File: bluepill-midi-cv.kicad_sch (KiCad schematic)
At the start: 8 parts

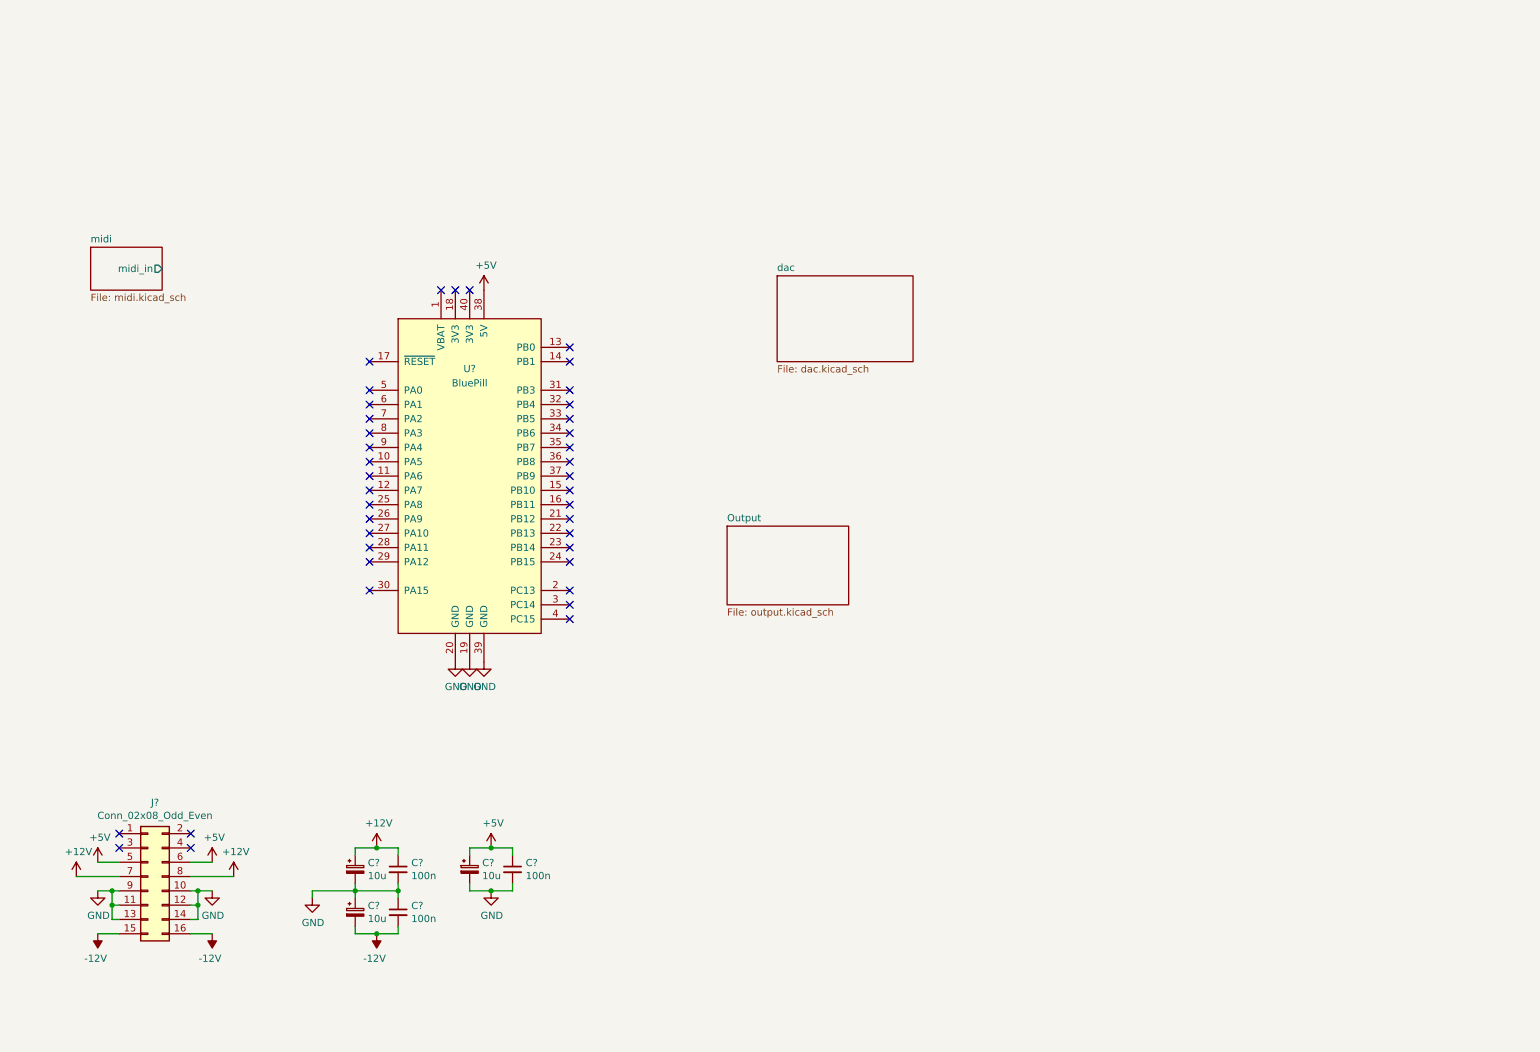
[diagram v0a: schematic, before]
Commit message: move schematic sub-sheets to main sheet
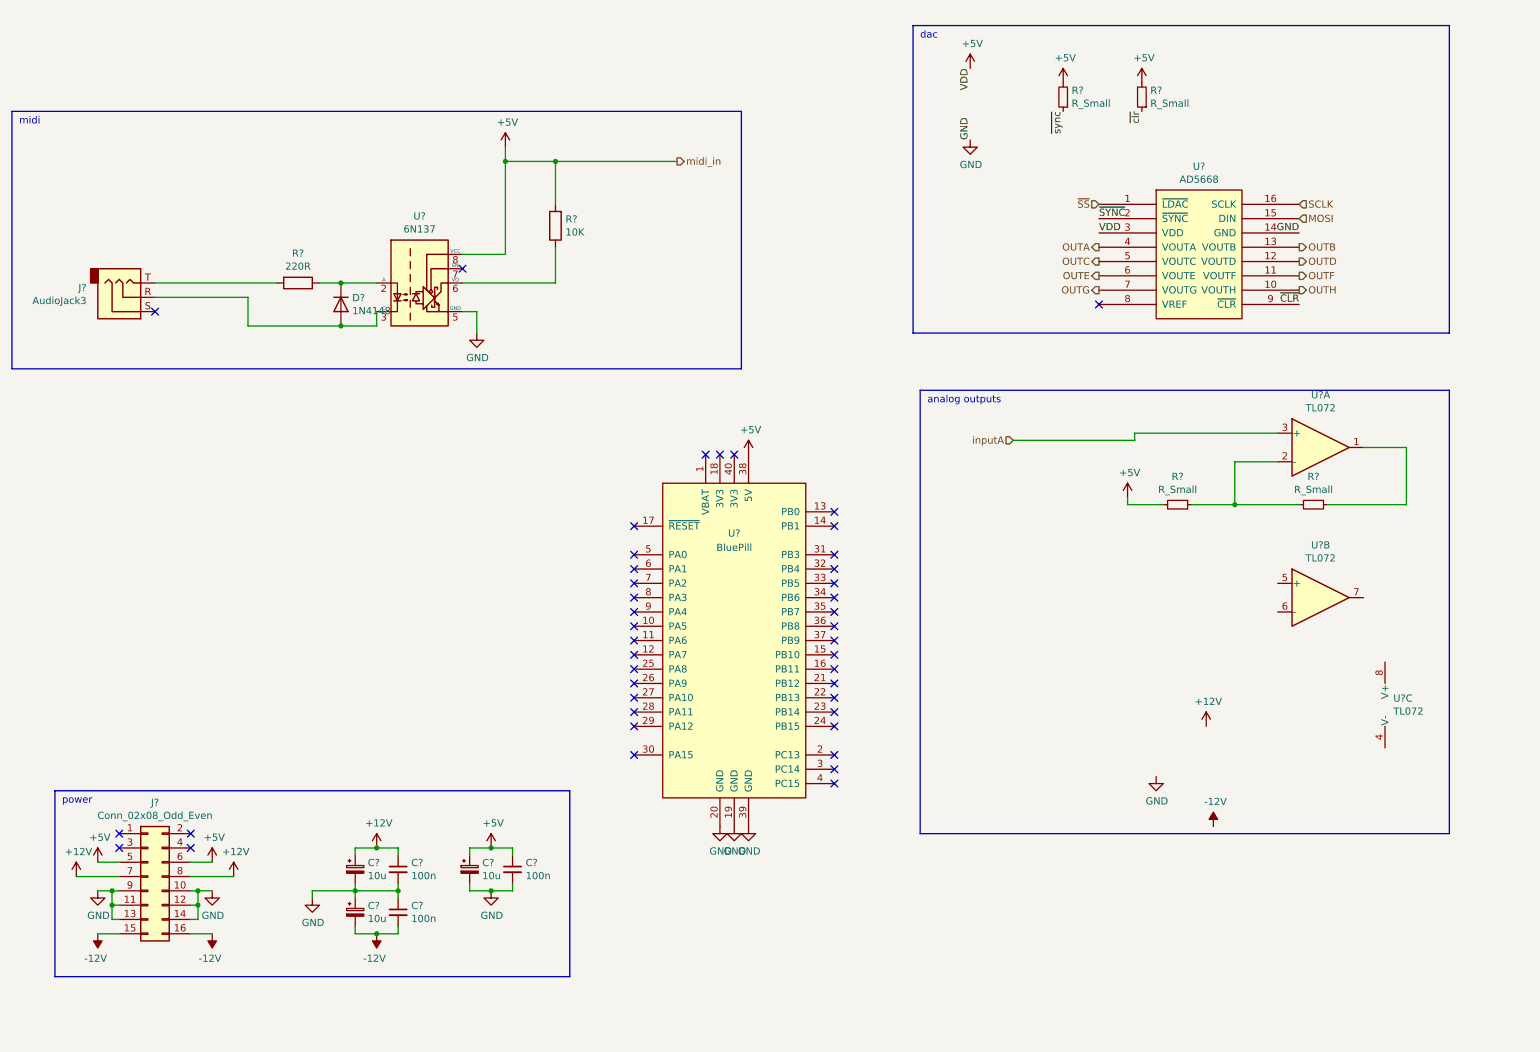
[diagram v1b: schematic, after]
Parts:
- added D?: 1N4148, Diode_SMD:D_0805_2012Metric_Pad1.15x1.40mm_HandSolder, symbol Diode:1N4148
- added J?: AudioJack3, Connector_Audio:Jack_3.5mm_QingPu_WQP-PJ398SM_Vertical_CircularHoles, symbol Connector:AudioJack3
- added R?: 10K, Resistor_SMD:R_0805_2012Metric_Pad1.15x1.40mm_HandSolder, symbol Device:R
- added R? (x4): R_Small, symbol Device:R_Small
- added R?: 220R, Resistor_SMD:R_0805_2012Metric_Pad1.15x1.40mm_HandSolder, symbol Device:R
- added U? (x3): TL072, symbol Amplifier_Operational:TL072
- added U?: AD5668, Package_SO:TSSOP-16-1EP_4.4x5mm_P0.65mm, symbol patchut:AD5668
- added U?: 6N137, Package_DIP:PowerIntegrations_SMD-8, symbol Isolator:6N137
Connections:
- net +5V: now also R?.2, R?.2, R?.2, R?.2, U?.3 (VDD), U?.8 (VCC)
- net GND: now also U?.14 (GND), U?.5 (GND)
- new net: R?.1, U?.6 (VO)
- new net: R?.1, U?.1
- new net: R?.1, R?.2, U?.2 (-)
- new net: D?.1 (K), R?.1, U?.2 (A)
- new net: D?.2 (A), J?.R, U?.3 (C)
- new net: J?.T, R?.2
- new net MOSI: U?.15 (DIN)
- new net OUTA: U?.4 (VOUTA)
- new net OUTB: U?.13 (VOUTB)
- new net OUTC: U?.5 (VOUTC)
- new net OUTD: U?.12 (VOUTD)
- new net OUTE: U?.6 (VOUTE)
- new net OUTF: U?.11 (VOUTF)
- new net OUTG: U?.7 (VOUTG)
- new net OUTH: U?.10 (VOUTH)
- new net SCLK: U?.16 (SCLK)
- new net inputA: U?.3 (+)
- new net ~{CLR}: U?.9 (~{CLR})
- new net ~{SS}: U?.1 (~{LDAC})
- new net ~{SYNC}: U?.2 (~{SYNC})
- new net ~{clr}: R?.1
- new net ~{sync}: R?.1
- no-connect marks 40 -> 43
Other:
- removed sheet Output
- removed sheet dac
- removed sheet midi
- note added: "analog outputs"
- note added: "dac"
- note added: "midi"
- note added: "power"
- moved on the sheet: U?

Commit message: finish 4 analog outs, more cleanup
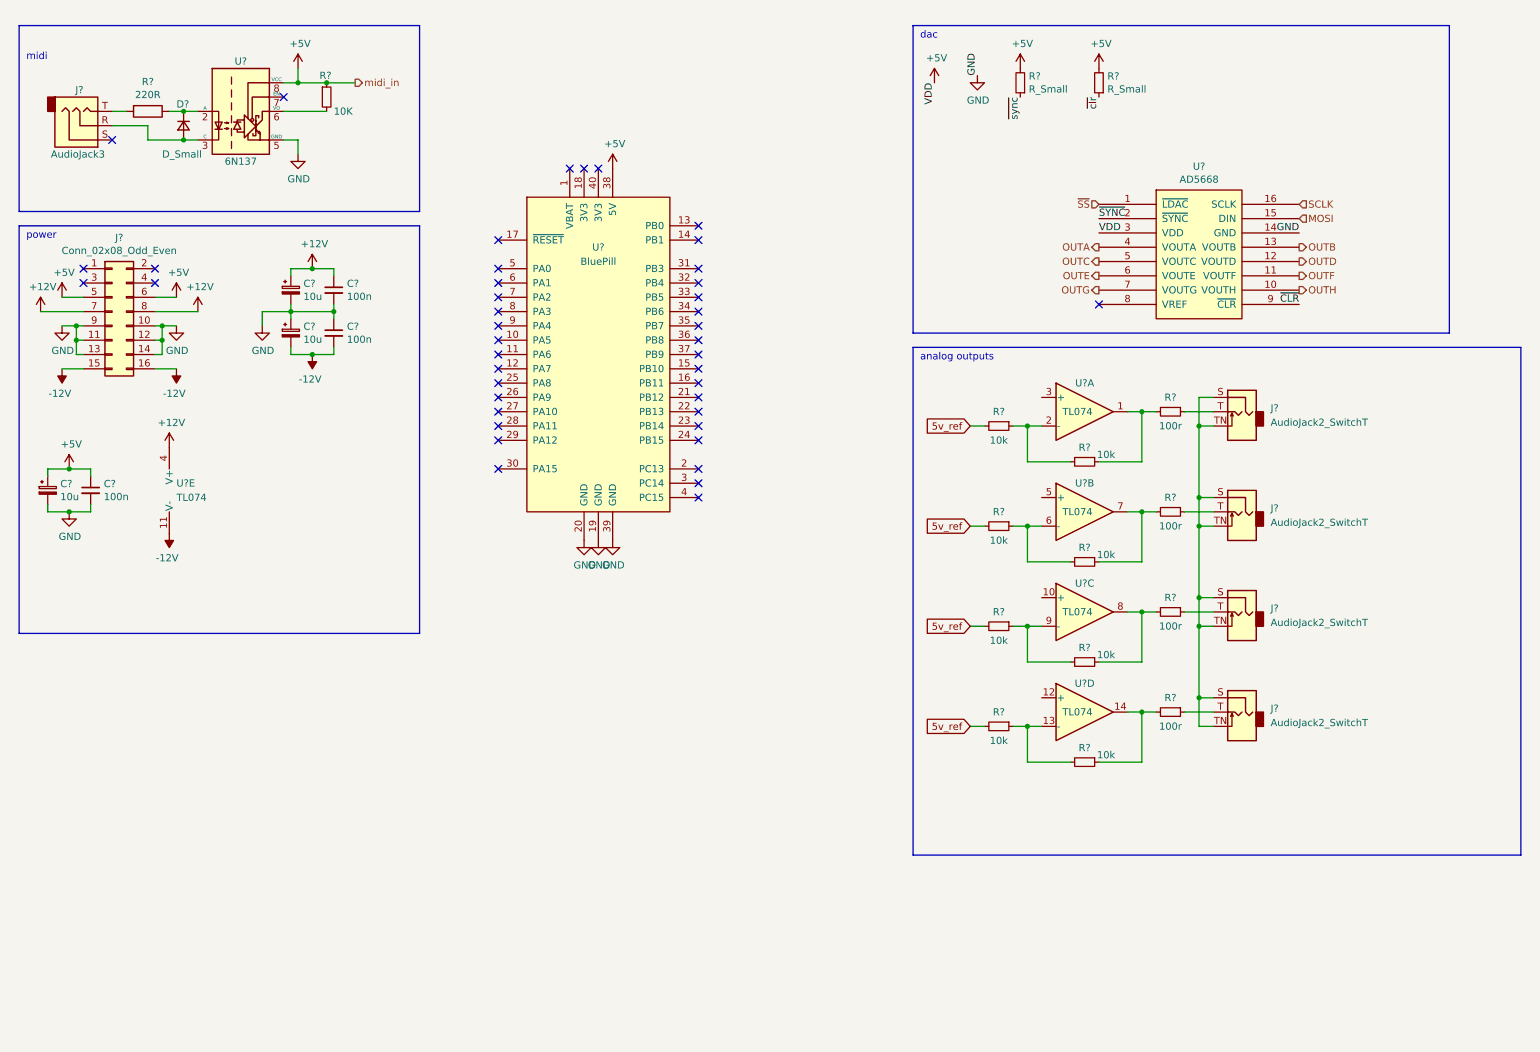
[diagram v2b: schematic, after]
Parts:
- removed D?: 1N4148, Diode_SMD:D_0805_2012Metric_Pad1.15x1.40mm_HandSolder, symbol Diode:1N4148
- removed R?: 10K, Resistor_SMD:R_0805_2012Metric_Pad1.15x1.40mm_HandSolder, symbol Device:R
- removed R?: R_Small, symbol Device:R_Small
- removed U? (x3): TL072, symbol Amplifier_Operational:TL072
- added D?: D_Small, symbol Device:D_Small
- added J? (x4): AudioJack2_SwitchT, symbol Connector:AudioJack2_SwitchT
- added R? (x7): 10k, symbol Device:R_Small
- added R? (x4): 100r, symbol Device:R_Small
- added R?: 10K, symbol Device:R_Small
- added U? (x5): TL074, symbol Amplifier_Operational:TL074
- R?: value R_Small -> 10k
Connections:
- net +12V: now also U?.4 (V+)
- net +5V: now also R?.1; no longer R?.2
- net -12V: now also U?.11 (V-)
- net at U?.6 (VO): now also R?.2
- net at R?.1: now also R?.2, U?.2 (-)
- net at R?.1, U?.2 (A): now also D?.1 (K)
- net at J?.R, U?.3 (C): now also D?.2 (A)
- new net: R?.1, R?.2, U?.1
- new net: J?.T, R?.1 (x4)
- new net: R?.1, R?.2, U?.8
- new net: R?.1, R?.2, U?.13 (-)
- new net: R?.1, R?.2, U?.9 (-)
- new net: R?.1, R?.2, U?.14
- new net: R?.1, R?.2, U?.6 (-)
- new net: R?.1, R?.2, U?.7
- new net: J?.S, J?.S, J?.S, J?.S, J?.TN, J?.TN, J?.TN, J?.TN
- new net 5v_ref: R?.2, R?.2, R?.2, R?.2
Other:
- moved on the sheet: C?, J?, R?, U?

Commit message: add all analog and digital outputs
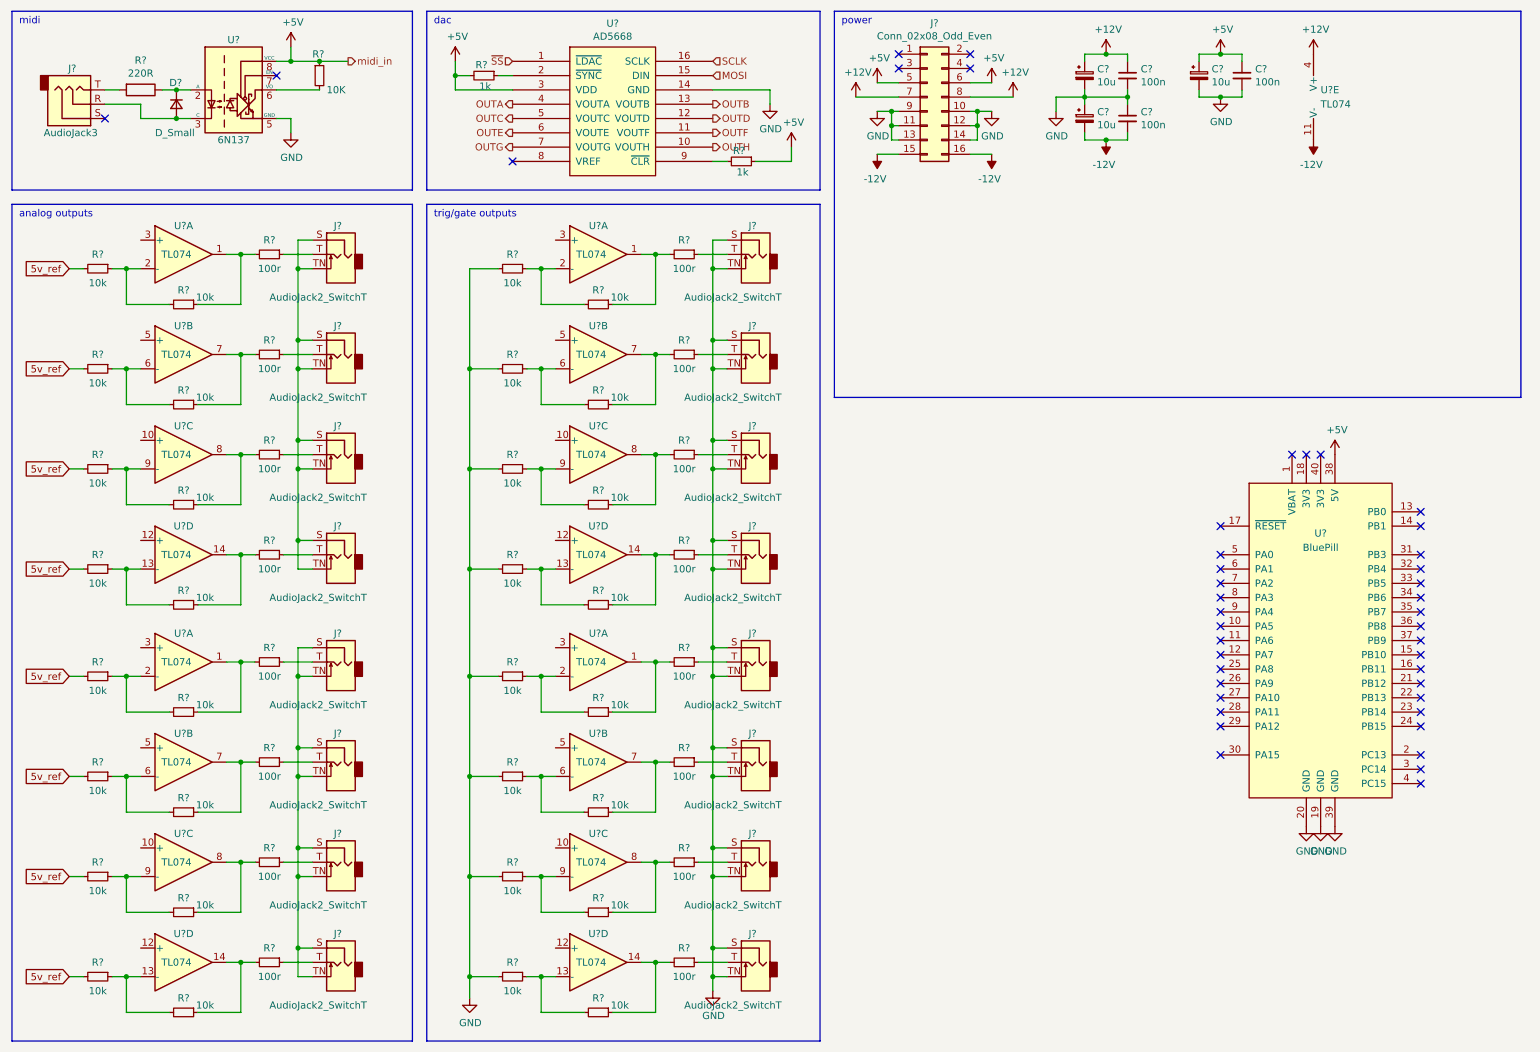
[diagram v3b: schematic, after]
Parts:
- removed R?: R_Small, symbol Device:R_Small
- added J? (x12): AudioJack2_SwitchT, symbol Connector:AudioJack2_SwitchT
- added R? (x12): 100r, symbol Device:R_Small
- added R? (x24): 10k, symbol Device:R_Small
- added R?: 1k, symbol Device:R_Small
- added U? (x12): TL074, symbol Amplifier_Operational:TL074
- R?: value R_Small -> 1k
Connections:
- net ~{sync} is gone; now on an unnamed net: R?.1
- net +5V: now also R?.1
- net 5v_ref: now also R?.2, R?.2, R?.2, R?.2
- net GND: now also J?.S, J?.S, J?.S, J?.S, J?.S, J?.S, J?.S, J?.S, J?.TN, J?.TN, J?.TN, J?.TN, J?.TN, J?.TN, J?.TN, J?.TN, R?.2, R?.2, R?.2, R?.2, R?.2, R?.2, R?.2, R?.2
- net ~{CLR}: no longer names the net of U?.9 (~{CLR})
- net ~{CLR}: now also R?.2
- net ~{SYNC}: no longer names the net of U?.2 (~{SYNC})
- new net: J?.T, R?.1 (x12)
- new net: R?.1, R?.2, U?.14 (x3)
- new net: R?.1, R?.2, U?.13 (-) (x3)
- new net: R?.1, R?.2, U?.1 (x3)
- new net: R?.1, R?.2, U?.2 (-) (x3)
- new net: R?.1, R?.2, U?.7 (x3)
- new net: R?.1, R?.2, U?.8 (x3)
- new net: R?.1, R?.2, U?.6 (-) (x3)
- new net: J?.S, J?.S, J?.S, J?.S, J?.TN, J?.TN, J?.TN, J?.TN
- new net: R?.1, R?.2, U?.9 (-) (x3)
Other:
- note added: "trig/gate outputs"
- moved on the sheet: C?, D?, J?, R?, U?, U?A, U?B, U?C, U?D, U?E

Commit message: disconnect jack switch connectors. add ground for analog output sleeve
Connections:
- net GND: now also J?.S, J?.S, J?.S, J?.S, J?.S, J?.S; no longer J?.TN, J?.TN, J?.TN, J?.TN, J?.TN, J?.TN, J?.TN, J?.TN
- now unconnected: J?.S, J?.S, J?.TN, J?.TN, J?.TN, J?.TN, J?.TN, J?.TN, J?.TN, J?.TN
- no-connect marks 43 -> 59
